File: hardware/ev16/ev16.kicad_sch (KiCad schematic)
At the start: 164 parts, among them CN1 Conn_05x02_Female, CN2 PJ-242, J1 USB_C_Receptacle, J10 Conn_01x03_Pin, J11 Conn_02x05_Counter_Clockwise, J2 Conn_01x02_Socket, J3 AudioJack4, J4 Conn_02x03_Odd_Even, J5 Conn_02x03_Odd_Even, J6 Conn_02x05_Counter_Clockwise, J7 Conn_02x05_Counter_Clockwise, J8 Conn_02x05_Counter_Clockwise, J9 Conn_02x05_Counter_Clockwise, Q1 2N7002, Q2 2N7002, SW1 SW_SPDT, SW2 SW_Push, SW3 SW_Push, SW4 SW_Push, SW5 SW_Push, SW6 SW_Push, SW7 SW_Push, U1 BQ21040DBV, U10 STM32F405RGTx, U2 USBLC6-2P6, U3 STM32F072CBTx, U4 CH340C, U5 TPS63060, U6 WM8960CGEFL/RV, U7 ESP32-S3-WROOM-1, U8 M24C02-RMN6TP, Y1 Crystal_GND24

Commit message: update 10u capacitors on boost converter to use C17024 part instead
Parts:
- C15, C16, C24, C27, C29, C30, C31, C35: JLCPCB Part # C83061 -> C17024

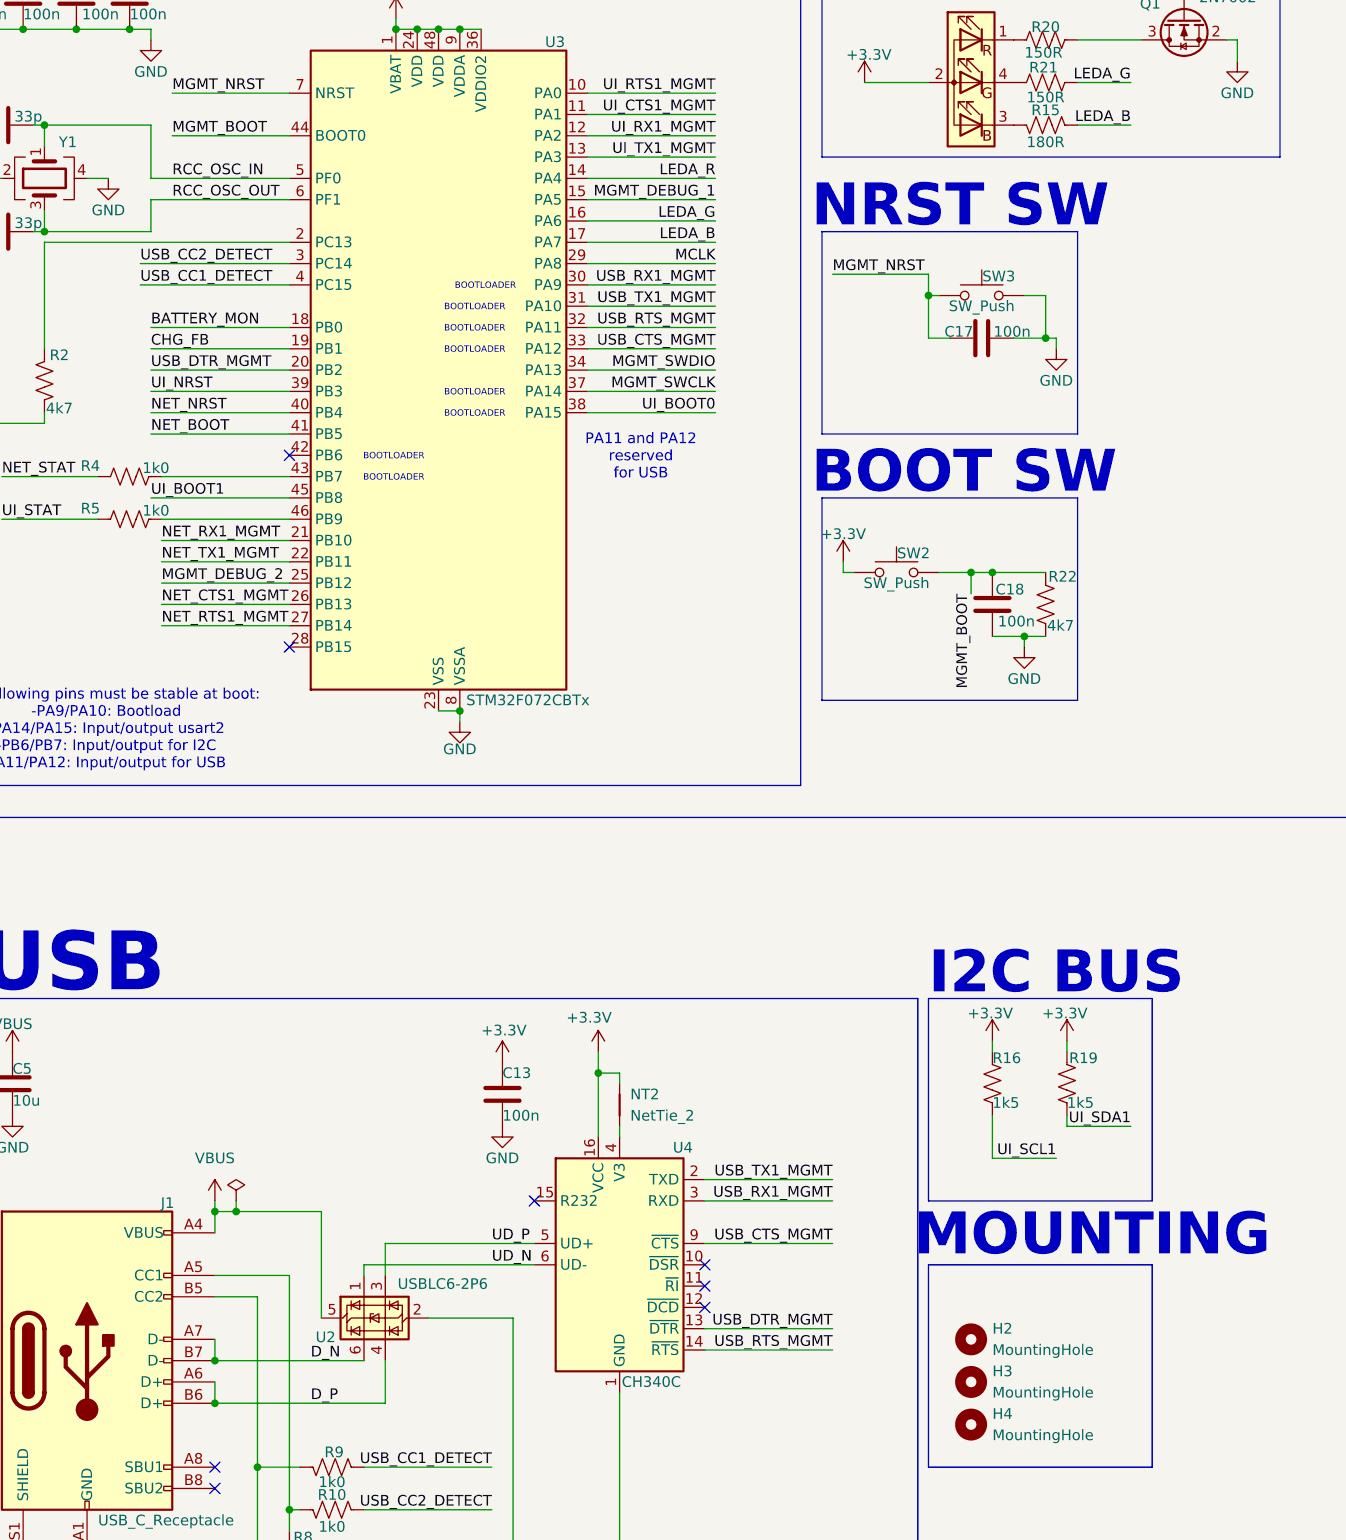
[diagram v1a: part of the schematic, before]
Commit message: feat: added auto reset mosfet to mgmt chip from usb
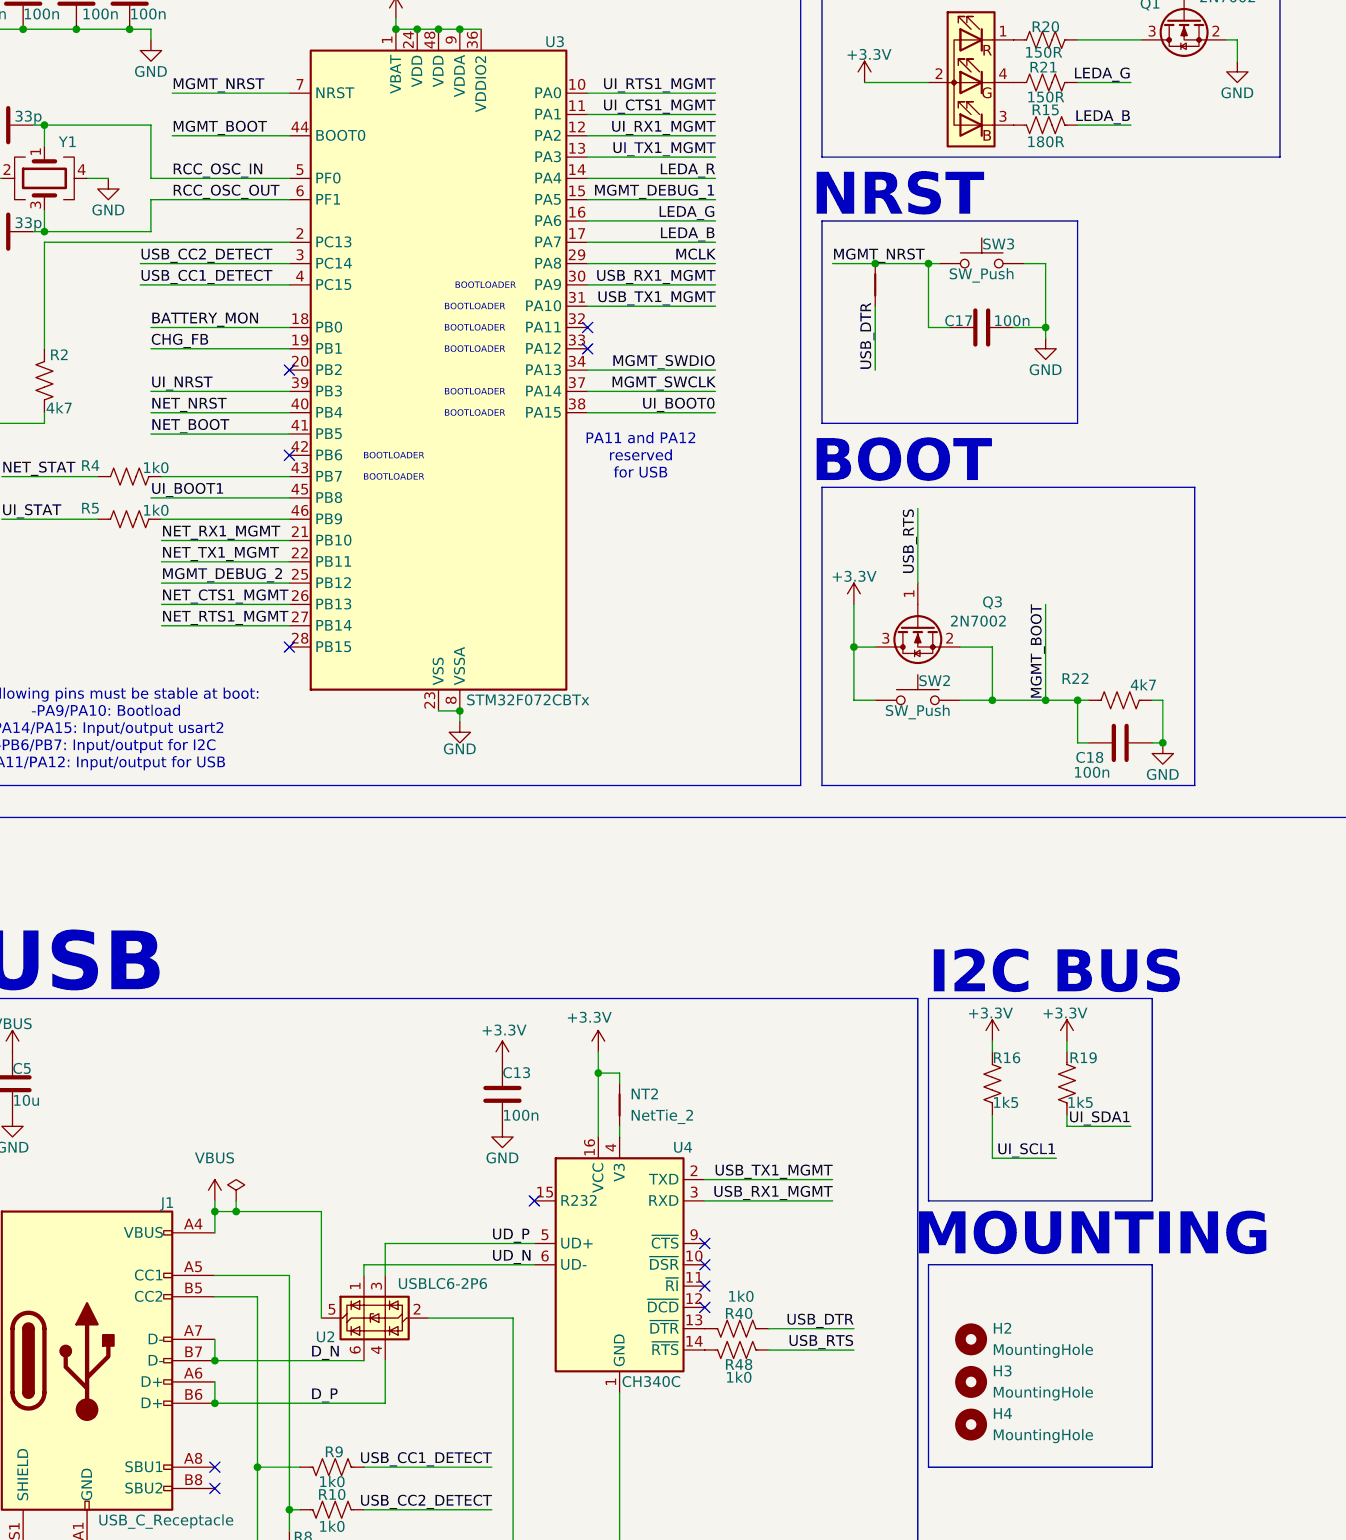
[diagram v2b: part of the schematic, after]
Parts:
- added NT3: NetTie_2, NetTie:NetTie-2_SMD_Pad0.5mm, symbol Device:NetTie_2
- added Q3: 2N7002, Package_TO_SOT_SMD:SOT-23, symbol Transistor_FET:2N7002
- added R40, R48: 1k0, Resistor_SMD:R_0402_1005Metric, symbol Device:R_US
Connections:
- net +3.3V: now also Q3.3 (D)
- net MGMT_BOOT: now also Q3.2 (S)
- net MGMT_NRST: now also NT3.2
- net USB_CTS_MGMT: no longer names the net of U3.33 (PA12)
- net USB_CTS_MGMT: no longer U4.9 (~{CTS})
- net USB_DTR_MGMT: no longer names the net of U4.13 (~{DTR})
- net USB_DTR_MGMT: now also R40.2; no longer U3.20 (PB2)
- net USB_RTS_MGMT: no longer names the net of U3.32 (PA11)
- net USB_RTS_MGMT: no longer U4.14 (~{RTS})
- new net: R48.2, U4.14 (~{RTS})
- new net USB_DTR: NT3.1, R40.1
- new net USB_RTS: Q3.1 (G), R48.1
- no-connect marks 53 -> 57
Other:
- note added: "BOOT"
- note added: "NRST"
- note removed: "BOOT SW"
- note removed: "NRST SW"
- moved on the sheet: C17, C18, R22, SW2, SW3

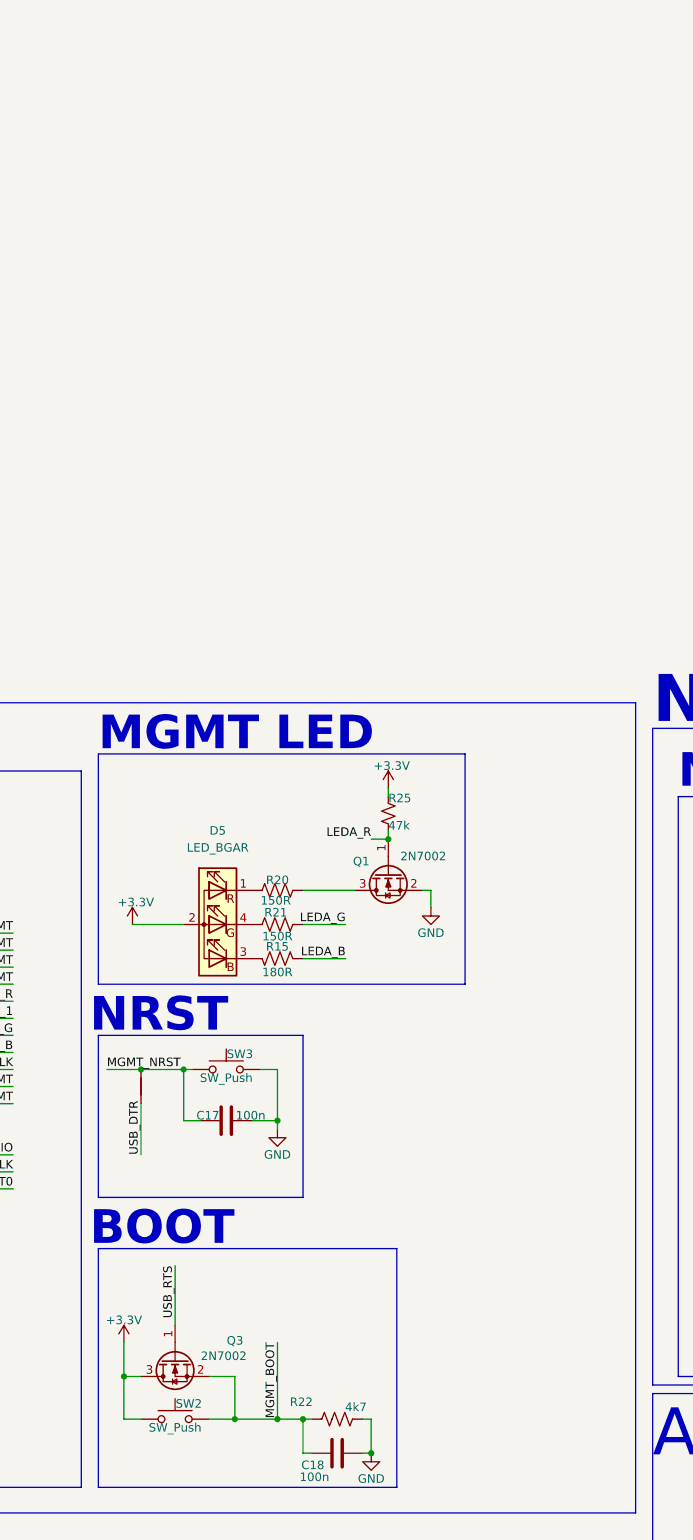
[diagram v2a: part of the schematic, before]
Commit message: fixed circuit for inverting mgmt boot signal from RTS
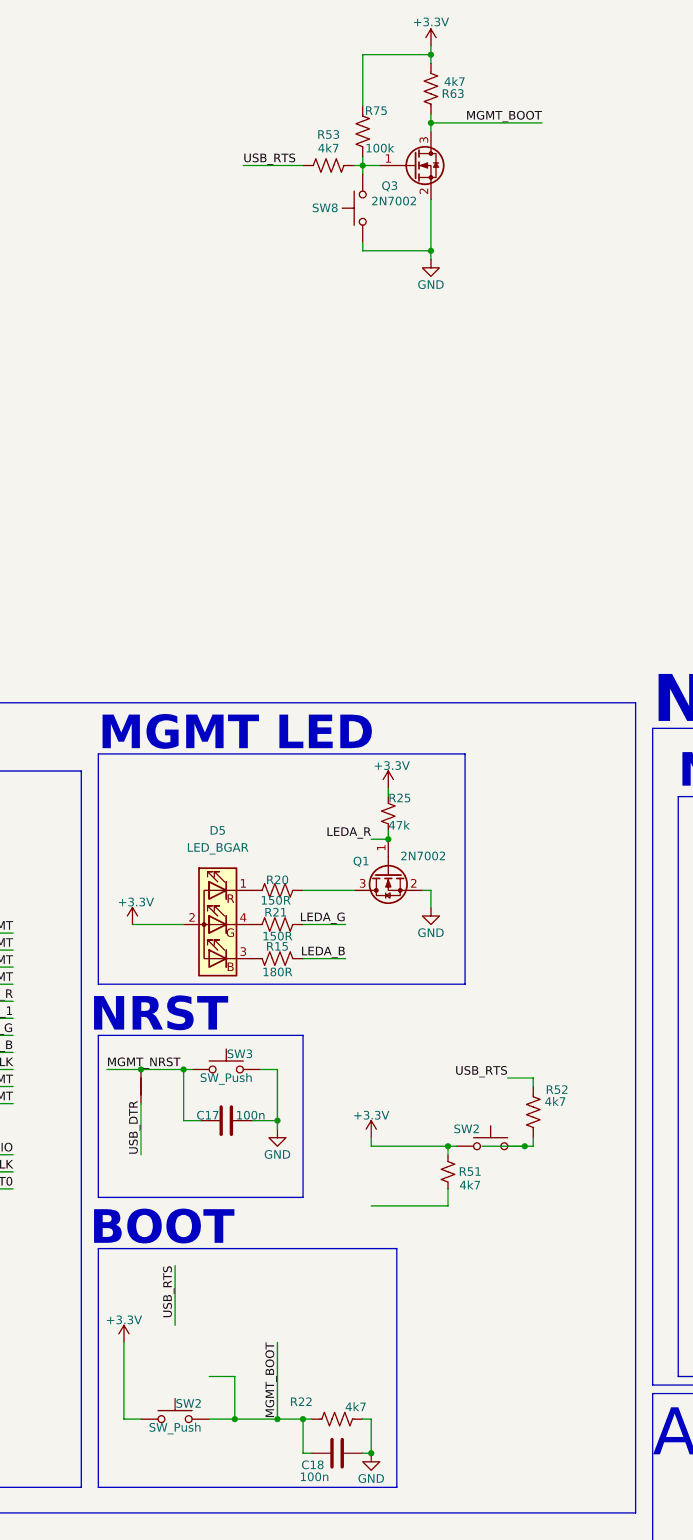
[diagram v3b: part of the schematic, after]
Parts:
- added R51: 4k7, Resistor_SMD:R_0402_1005Metric, symbol Device:R_Small_US
- added R52, R53, R63: 4k7, Resistor_SMD:R_0402_1005Metric, symbol Device:R_US
- added R75: 100k, Resistor_SMD:R_0402_1005Metric, symbol Device:R_US
- added SW2, SW8: SW_Push, Hactar_Footprints:KEY-SMD_4P-L4.2-W3.2-P2.20-LS4.6, symbol Hactar_Symbols:SW_Push_4C
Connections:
- net +3.3V: now also R51.2, R63.2, R75.2, SW2.1, SW2.2; no longer Q3.3 (D)
- net GND: now also Q3.2 (S), SW8.1, SW8.2
- net MGMT_BOOT: now also Q3.3 (D), R63.1; no longer Q3.2 (S)
- net USB_RTS: now also R52.1, R53.1; no longer Q3.1 (G)
- new net: Q3.1 (G), R53.2, R75.1, SW8.3, SW8.4
- new net: R52.2, SW2.3, SW2.4
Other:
- moved on the sheet: Q3

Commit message: production generator push
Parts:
- removed C18: 100n, Capacitor_SMD:C_0402_1005Metric, symbol Device:C
- removed R22, R52, R53: 4k7, Resistor_SMD:R_0402_1005Metric, symbol Device:R_US
- removed R48: 1k0, Resistor_SMD:R_0402_1005Metric, symbol Device:R_US
- removed R51: 4k7, Resistor_SMD:R_0402_1005Metric, symbol Device:R_Small_US
- removed SW2 (x2): SW_Push, Hactar_Footprints:KEY-SMD_4P-L4.2-W3.2-P2.20-LS4.6, symbol Hactar_Symbols:SW_Push_4C
- added R51: 4k7, Resistor_SMD:R_0402_1005Metric, symbol Device:R_US
- renumbered R63 to R22, SW8 to SW2
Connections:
- net USB_DTR: now also R40.2, U4.13 (~{DTR}); no longer NT3.1, R40.1
- net USB_RTS: now also U4.14 (~{RTS}), R51.1
- net at Q3.1 (G), R75.1, SW2.3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: now also R51.2
- new net: NT3.1, R40.1
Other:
- moved on the sheet: C17, Q3, R22, R40, R75, SW2, SW3
